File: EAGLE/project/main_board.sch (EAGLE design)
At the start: 5 parts, among them U1 RASPBERRY_PI_4B_4GB, U2 2472, X1 MKDSN1,5/3-5,08, X2 MKDSN1,5/3-5,08

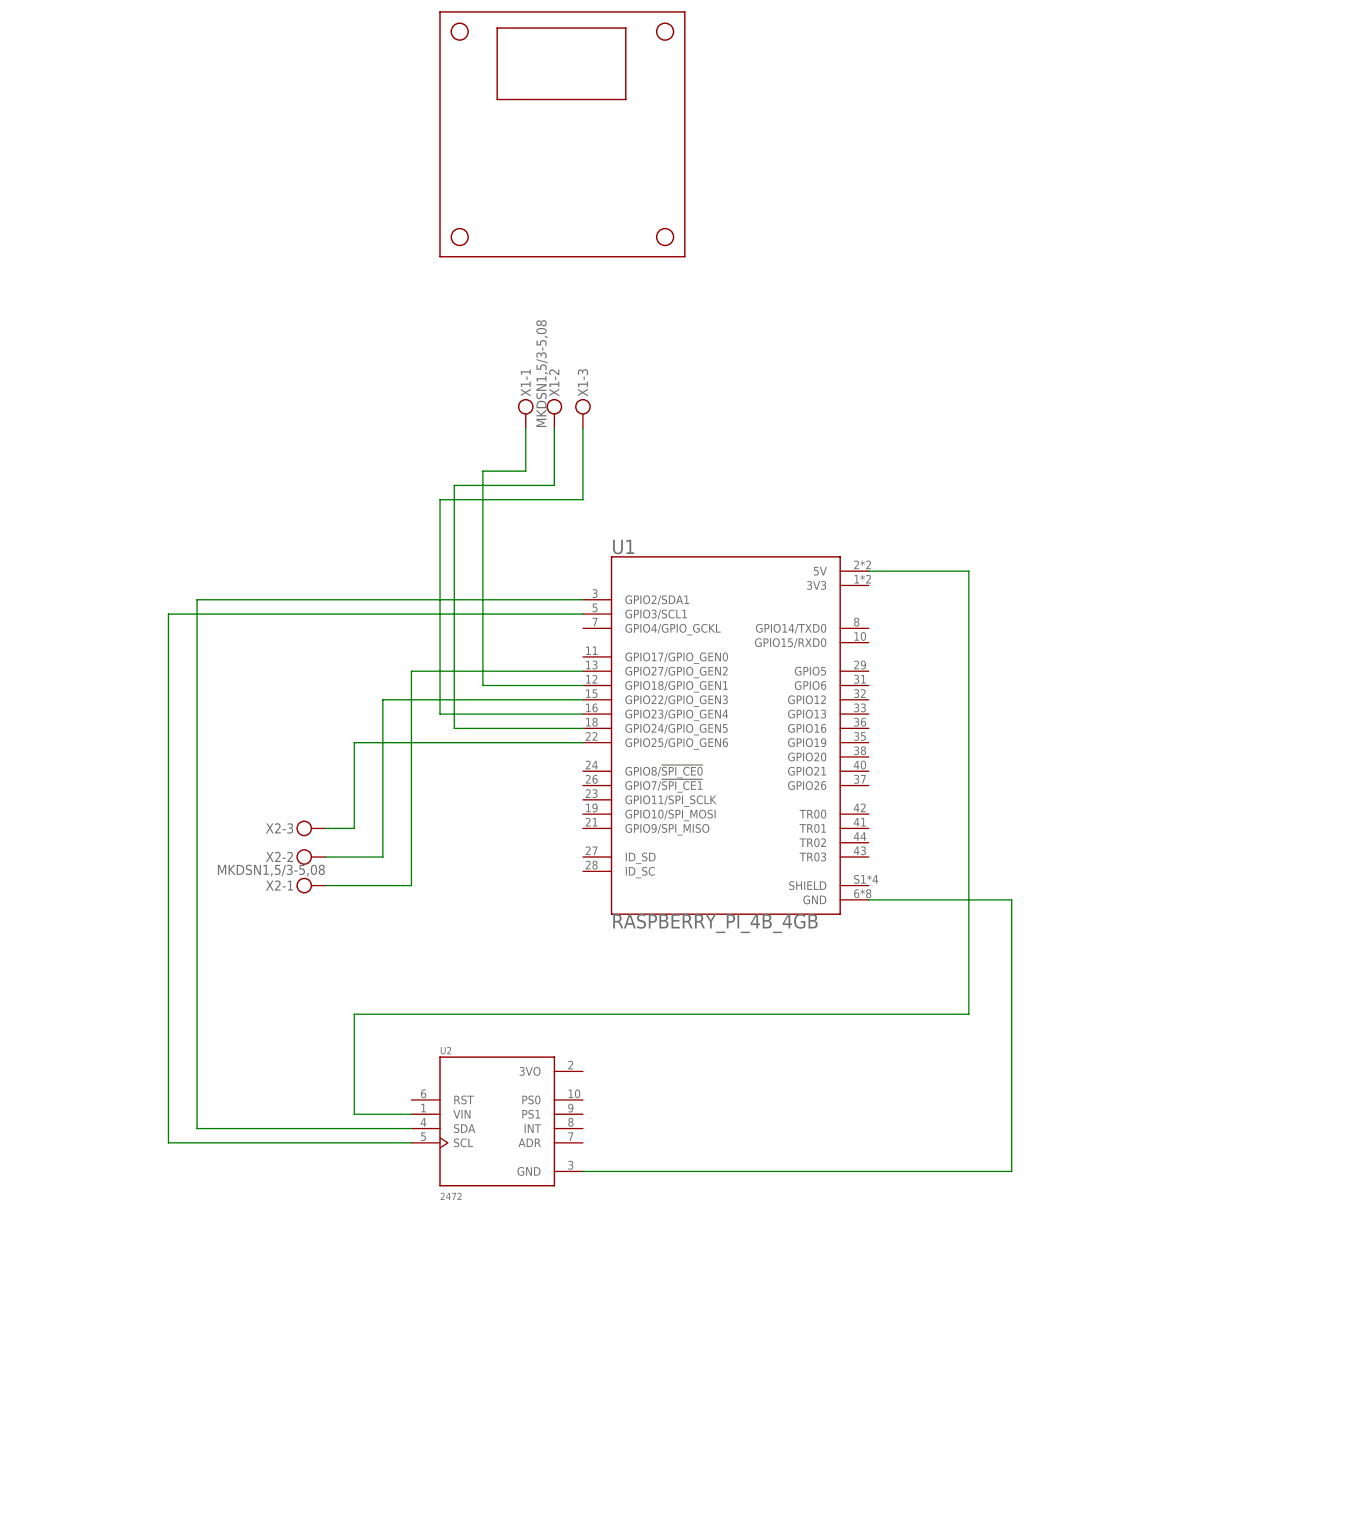
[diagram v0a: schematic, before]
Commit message: design main board PCB by EAGLE
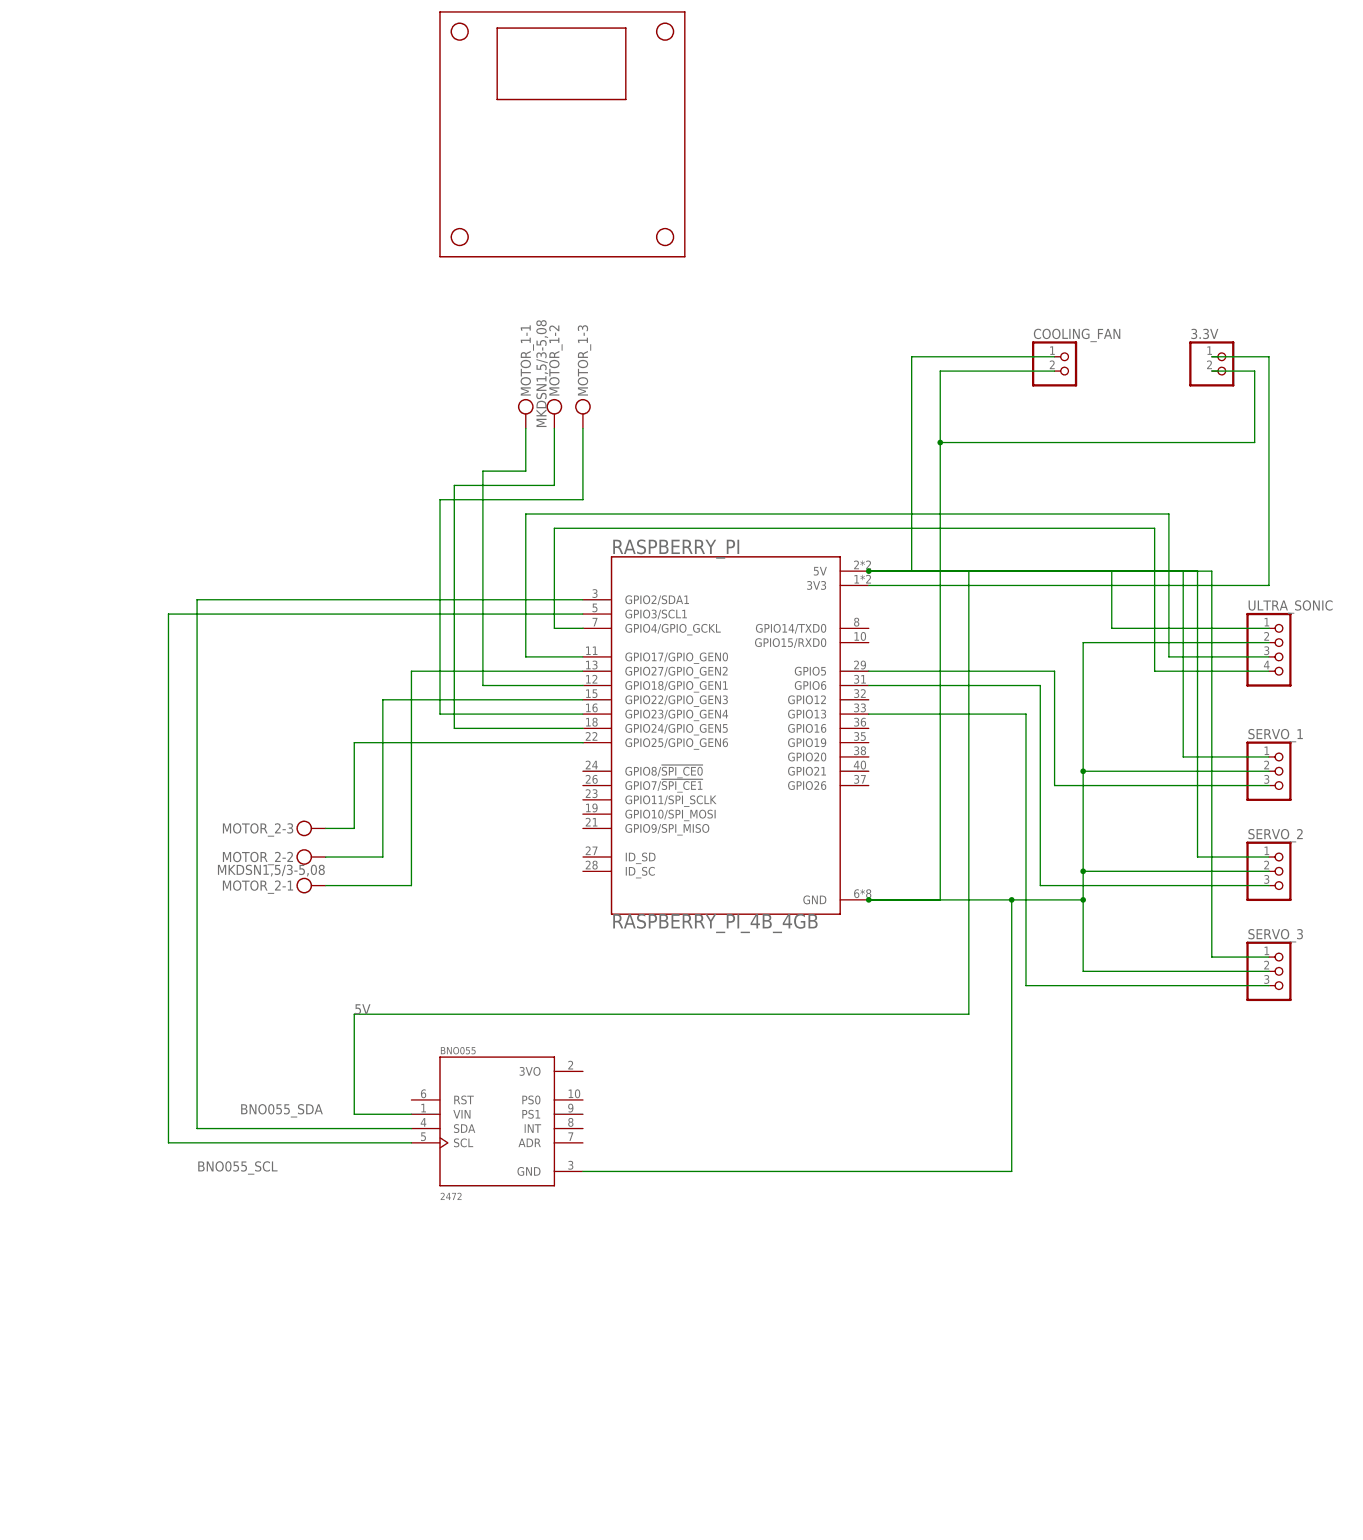
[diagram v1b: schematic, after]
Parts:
- added 3.3V, COOLING_FAN: (no value), pinhead:PINHD-1X2
- added SERVO_1, SERVO_2, SERVO_3: (no value), pinhead:PINHD-1X3
- added ULTRA_SONIC: (no value), pinhead:PINHD-1X4
- renumbered U1 to RASPBERRY_PI, U2 to BNO055, X1 to MOTOR_1, X2 to MOTOR_2
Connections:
- net N$10 renamed ENB
- net N$3 renamed BNO055_SDA
- net N$4 renamed BNO055_SCL
- net N$5 renamed ENA
- net N$6 renamed IN1
- net N$7 renamed IN2
- net N$8 renamed IN3
- net N$9 renamed IN4
- removed net N$1: BNO055.VIN, RASPBERRY_PI.5V
- removed net N$2: BNO055.GND, RASPBERRY_PI.GND
- new net 3.3V: 3.3V.1, RASPBERRY_PI.3V3
- new net 5V: BNO055.VIN, COOLING_FAN.1, RASPBERRY_PI.5V, SERVO_1.1, SERVO_2.1, SERVO_3.1, ULTRA_SONIC.1
- new net GND: 3.3V.2, BNO055.GND, COOLING_FAN.2, RASPBERRY_PI.GND, SERVO_1.2, SERVO_2.2, SERVO_3.2, ULTRA_SONIC.2
- new net PWM_SERVO_1: RASPBERRY_PI.GPIO5, SERVO_1.3
- new net PWM_SERVO_2: RASPBERRY_PI.GPIO6, SERVO_2.3
- new net PWM_SERVO_3: RASPBERRY_PI.GPIO13, SERVO_3.3
- new net ULTRA_SONIC_1: RASPBERRY_PI.GPIO4/GPIO_GCKL, ULTRA_SONIC.4
- new net ULTRA_SONIC_2: RASPBERRY_PI.GPIO17/GPIO_GEN0, ULTRA_SONIC.3

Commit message: update main board
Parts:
- added GPS: (no value), pinhead:PINHD-1X4
- renumbered COOLING_FAN to FAN
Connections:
- new net RX: GPS.3, RASPBERRY_PI.GPIO14/TXD0
- new net TX: GPS.2, RASPBERRY_PI.GPIO15/RXD0
- net 5V: now also GPS.4
- net GND: now also GPS.1
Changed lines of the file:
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@@
 </variantdefs>
 <classes>
-<class number="0" name="default" width="0.45" drill="0">
+<class number="0" name="default" width="0.5" drill="0">
 <clearance class="0" value="0.254"/>
 </class>
-<class number="1" name="5V/3,3V/GND" width="0.5" drill="0">
-<clearance class="1" value="0.254"/>
+<class number="1" name="5V/3,3V/GND" width="1" drill="0">
+<clearance class="1" value="0.381"/>
 </class>
 </classes>
@@
 <part name="SERVO_2" library="pinhead" library_urn="urn:adsk.eagle:library:325" deviceset="PINHD-1X3" device="" package3d_urn="urn:adsk.eagle:package:22458/2"/>
 <part name="SERVO_3" library="pinhead" library_urn="urn:adsk.eagle:library:325" deviceset="PINHD-1X3" device="" package3d_urn="urn:adsk.eagle:package:22458/2"/>
-<part name="COOLING_FAN" library="pinhead" library_urn="urn:adsk.eagle:library:325" deviceset="PINHD-1X2" device="" package3d_urn="urn:adsk.eagle:package:22435/2"/>
+<part name="FAN" library="pinhead" library_urn="urn:adsk.eagle:library:325" deviceset="PINHD-1X2" device="" package3d_urn="urn:adsk.eagle:package:22435/2"/>
 <part name="3.3V" library="pinhead" library_urn="urn:adsk.eagle:library:325" deviceset="PINHD-1X2" device="" package3d_urn="urn:adsk.eagle:package:22435/2"/>
+<part name="GPS" library="pinhead" library_urn="urn:adsk.eagle:library:325" deviceset="PINHD-1X4" device="" package3d_urn="urn:adsk.eagle:package:22407/2"/>
 </parts>
 <sheets>
@@
 <attribute name="VALUE" x="92.71" y="-48.26" size="1.778" layer="96"/>
 </instance>
-<instance part="COOLING_FAN" gate="G$1" x="60.96" y="66.04" smashed="yes">
+<instance part="FAN" gate="G$1" x="60.96" y="66.04" smashed="yes">
 <attribute name="NAME" x="54.61" y="71.755" size="1.778" layer="95"/>
 <attribute name="VALUE" x="54.61" y="60.96" size="1.778" layer="96"/>
@@
 <attribute name="NAME" x="82.55" y="71.755" size="1.778" layer="95"/>
 <attribute name="VALUE" x="82.55" y="60.96" size="1.778" layer="96"/>
+</instance>
+<instance part="GPS" gate="A" x="99.06" y="-71.12" smashed="yes">
+<attribute name="NAME" x="92.71" y="-62.865" size="1.778" layer="95"/>
+<attribute name="VALUE" x="92.71" y="-78.74" size="1.778" layer="96"/>
 </instance>
 </instances>
@@
 <wire x1="25.4" y1="30.48" x2="33.02" y2="30.48" width="0.1524" layer="91"/>
 <wire x1="33.02" y1="30.48" x2="33.02" y2="68.58" width="0.1524" layer="91"/>
-<pinref part="COOLING_FAN" gate="G$1" pin="1"/>
+<pinref part="FAN" gate="G$1" pin="1"/>
 <wire x1="33.02" y1="68.58" x2="58.42" y2="68.58" width="0.1524" layer="91"/>
 <wire x1="25.4" y1="30.48" x2="81.28" y2="30.48" width="0.1524" layer="91"/>
@@
 <pinref part="SERVO_3" gate="A" pin="1"/>
 <wire x1="86.36" y1="-38.1" x2="96.52" y2="-38.1" width="0.1524" layer="91"/>
+<wire x1="25.4" y1="30.48" x2="30.48" y2="30.48" width="0.1524" layer="91"/>
+<wire x1="30.48" y1="30.48" x2="30.48" y2="-73.66" width="0.1524" layer="91"/>
+<pinref part="GPS" gate="A" pin="4"/>
+<wire x1="30.48" y1="-73.66" x2="96.52" y2="-73.66" width="0.1524" layer="91"/>
 </segment>
 </net>
@@
 <wire x1="38.1" y1="-27.94" x2="38.1" y2="53.34" width="0.1524" layer="91"/>
 <junction x="25.4" y="-27.94"/>
-<pinref part="COOLING_FAN" gate="G$1" pin="2"/>
+<pinref part="FAN" gate="G$1" pin="2"/>
 <wire x1="38.1" y1="53.34" x2="38.1" y2="66.04" width="0.1524" layer="91"/>
 <wire x1="38.1" y1="66.04" x2="58.42" y2="66.04" width="0.1524" layer="91"/>
@@
 <pinref part="3.3V" gate="G$1" pin="2"/>
 <wire x1="93.98" y1="66.04" x2="86.36" y2="66.04" width="0.1524" layer="91"/>
+<pinref part="GPS" gate="A" pin="1"/>
+<wire x1="25.4" y1="-27.94" x2="25.4" y2="-66.04" width="0.1524" layer="91"/>
+<wire x1="25.4" y1="-66.04" x2="96.52" y2="-66.04" width="0.1524" layer="91"/>
 </segment>
 </net>
@@
 </segment>
 </net>
-<net name="3.3V" class="0">
+<net name="3.3V" class="1">
 <segment>
 <pinref part="RASPBERRY_PI" gate="G$1" pin="3V3"/>
@@
 </segment>
 </net>
+<net name="TX" class="0">
+<segment>
+<pinref part="RASPBERRY_PI" gate="G$1" pin="GPIO15/RXD0"/>
+<wire x1="25.4" y1="17.78" x2="33.02" y2="17.78" width="0.1524" layer="91"/>
+<wire x1="33.02" y1="17.78" x2="33.02" y2="-68.58" width="0.1524" layer="91"/>
+<pinref part="GPS" gate="A" pin="2"/>
+<wire x1="33.02" y1="-68.58" x2="96.52" y2="-68.58" width="0.1524" layer="91"/>
+</segment>
+</net>
+<net name="RX" class="0">
+<segment>
+<pinref part="RASPBERRY_PI" gate="G$1" pin="GPIO14/TXD0"/>
+<wire x1="25.4" y1="20.32" x2="35.56" y2="20.32" width="0.1524" layer="91"/>
+<wire x1="35.56" y1="20.32" x2="35.56" y2="-71.12" width="0.1524" layer="91"/>
+<pinref part="GPS" gate="A" pin="3"/>
+<wire x1="35.56" y1="-71.12" x2="96.52" y2="-71.12" width="0.1524" layer="91"/>
+</segment>
+</net>
